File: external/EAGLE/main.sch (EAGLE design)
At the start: 3 parts, among them IC1 AD590ZR

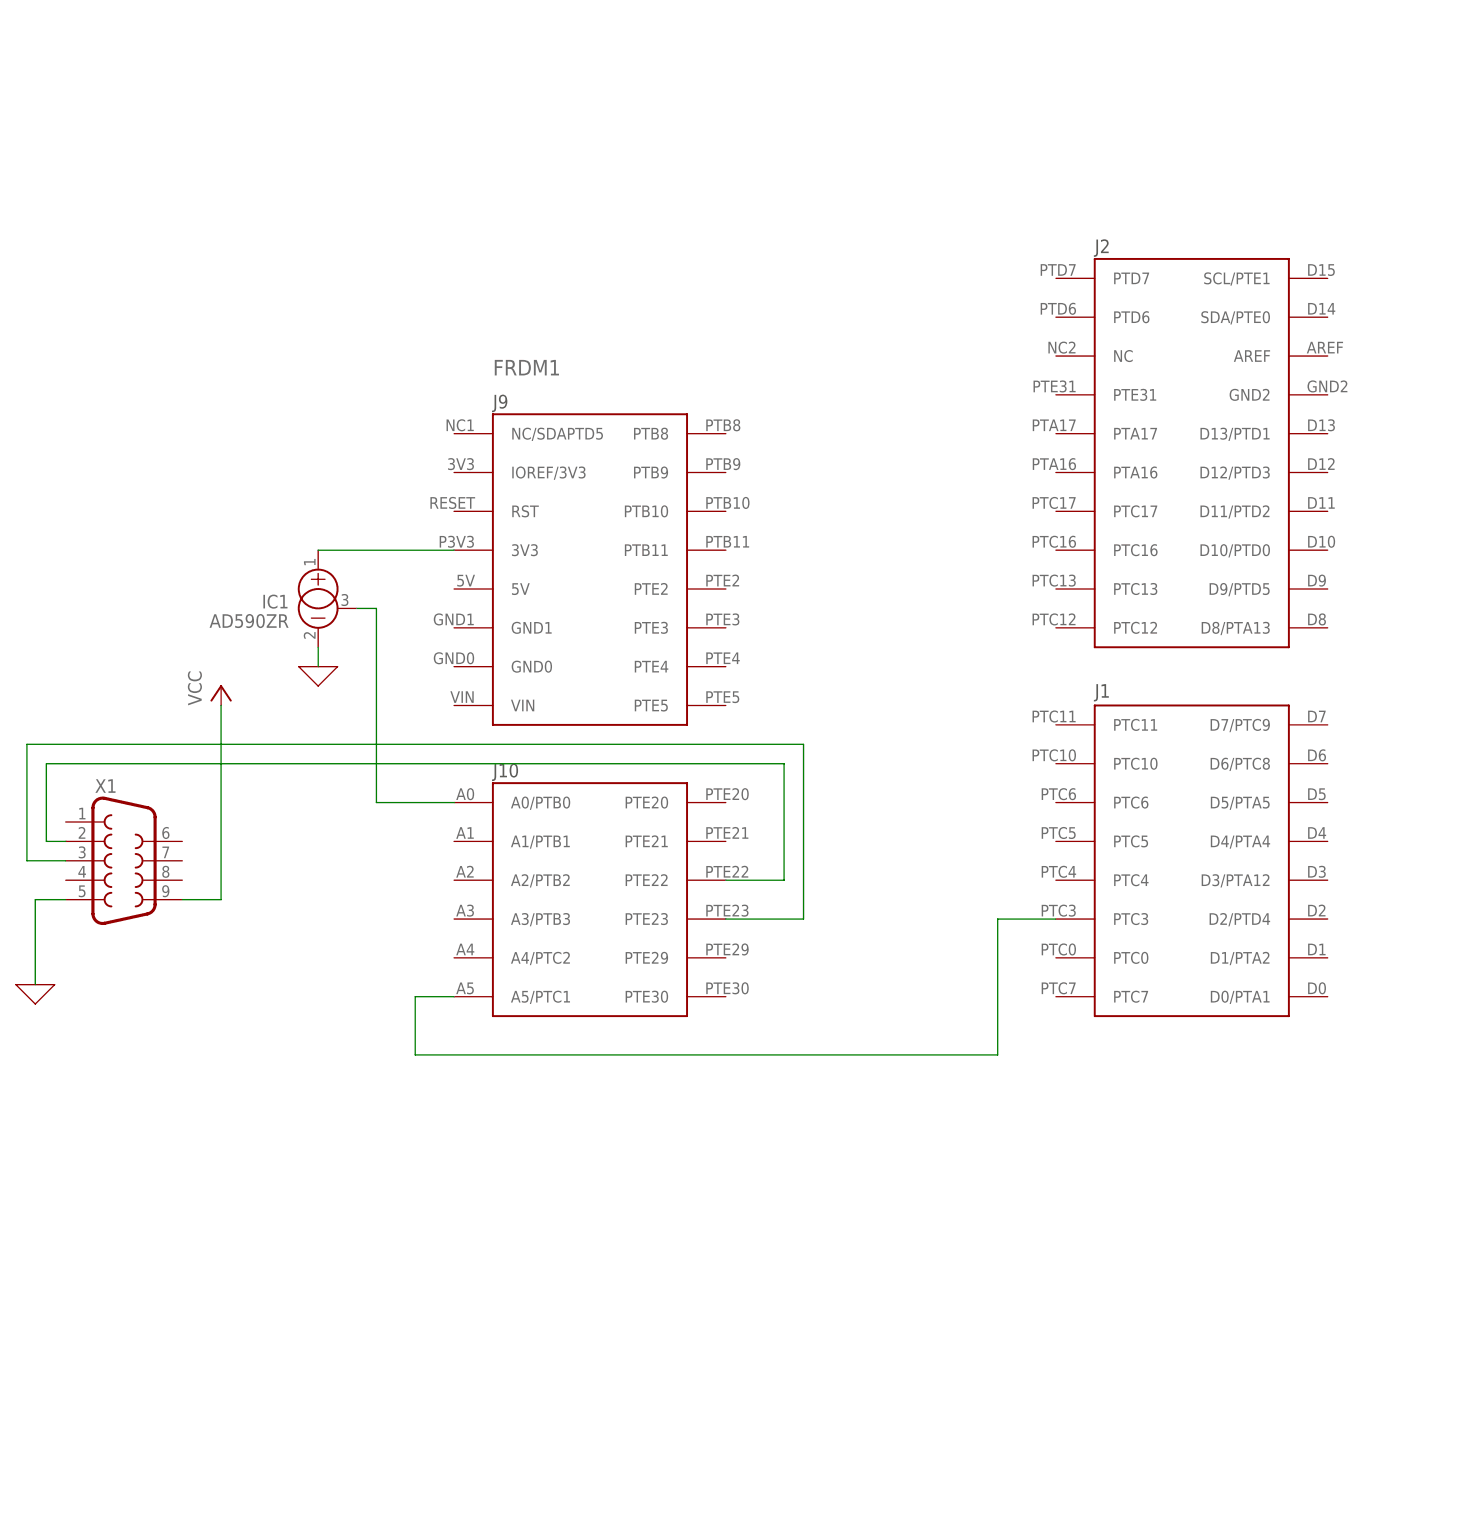
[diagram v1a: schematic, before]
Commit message: Updating the EAGLE schematic
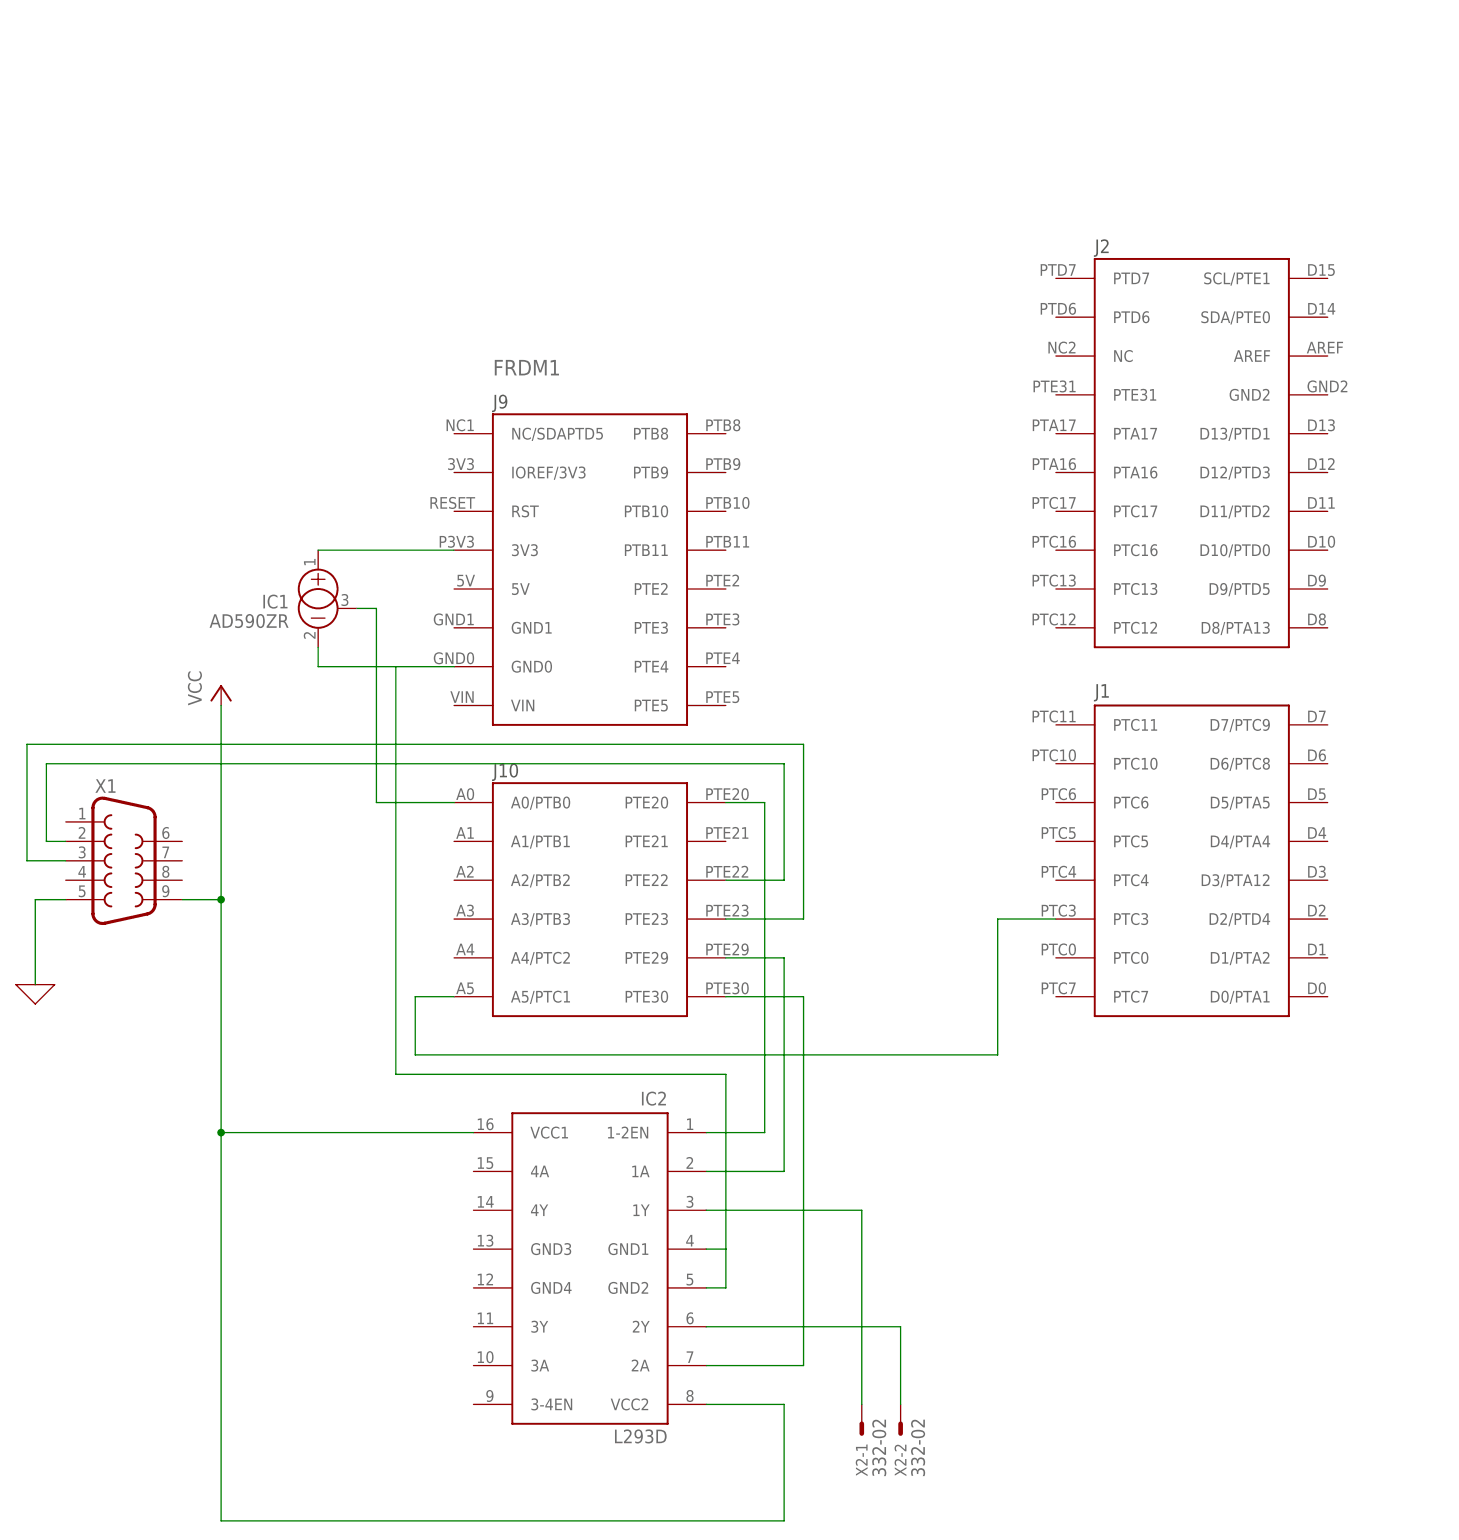
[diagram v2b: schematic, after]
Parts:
- added IC2: L293D, st-microelectronics:L293D
- added X2: 332-02, con-garry:332-02
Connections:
- new net N$10: IC2.2Y, X2-2.S
- new net N$11: FRDM1.GND0, IC1.-, IC2.GND1, IC2.GND2
- new net N$5: IC2.1Y, X2-1.S
- new net N$7: FRDM1.PTE20, IC2.1-2EN
- new net N$8: FRDM1.PTE29, IC2.1A
- new net N$9: FRDM1.PTE30, IC2.2A
- net 0: no longer IC1.-
- net VCC: now also IC2.VCC1, IC2.VCC2
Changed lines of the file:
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@@
 <part name="P+1" library="supply1" library_urn="urn:adsk.eagle:library:371" deviceset="VCC" device=""/>
 <part name="IC1" library="linear" library_urn="urn:adsk.eagle:library:262" deviceset="AD590ZR" device="" package3d_urn="urn:adsk.eagle:package:16416/2"/>
-<part name="X_2" library="ngspice-simulation" library_urn="urn:adsk.eagle:library:527439" deviceset="GND" device=""/>
+<part name="IC2" library="st-microelectronics" library_urn="urn:adsk.eagle:library:368" deviceset="L293D" device="" package3d_urn="urn:adsk.eagle:package:26820/1"/>
+<part name="X2" library="con-garry" library_urn="urn:adsk.eagle:library:147" deviceset="332-02" device="" package3d_urn="urn:adsk.eagle:package:6810/1"/>
 </parts>
 <sheets>
@@
 <attribute name="VALUE" x="44.45" y="-12.7" size="1.778" layer="96" rot="MR0"/>
 </instance>
-<instance part="X_2" gate="G$1" x="48.26" y="-17.78" smashed="yes"/>
+<instance part="IC2" gate="G$1" x="83.82" y="-96.52" smashed="yes" rot="MR0">
+<attribute name="NAME" x="93.98" y="-75.184" size="1.778" layer="95" rot="MR0"/>
+<attribute name="VALUE" x="93.98" y="-119.38" size="1.778" layer="96" rot="MR0"/>
+</instance>
+<instance part="X2" gate="-1" x="119.38" y="-116.84" smashed="yes" rot="R270">
+<attribute name="NAME" x="118.618" y="-119.38" size="1.524" layer="95" rot="R270"/>
+<attribute name="VALUE" x="120.777" y="-116.078" size="1.778" layer="96" rot="R270"/>
+</instance>
+<instance part="X2" gate="-2" x="124.46" y="-116.84" smashed="yes" rot="R270">
+<attribute name="NAME" x="123.698" y="-119.38" size="1.524" layer="95" rot="R270"/>
+<attribute name="VALUE" x="125.857" y="-116.078" size="1.778" layer="96" rot="R270"/>
+</instance>
 </instances>
 <busses>
@@
 <wire x1="11.24940625" y1="-48.26" x2="15.24" y2="-48.26" width="0.1524" layer="91"/>
 </segment>
-<segment>
-<pinref part="X_2" gate="G$1" pin="0"/>
-<pinref part="IC1" gate="A" pin="-"/>
-<wire x1="48.26" y1="-17.78" x2="48.26" y2="-15.24" width="0.1524" layer="91"/>
-</segment>
 </net>
 <net name="VCC" class="0">
@@
 <wire x1="30.48" y1="-48.26" x2="35.56" y2="-48.26" width="0.1524" layer="91"/>
 <wire x1="35.56" y1="-48.26" x2="35.56" y2="-22.86" width="0.1524" layer="91"/>
+<pinref part="IC2" gate="G$1" pin="VCC1"/>
+<wire x1="35.56" y1="-48.26" x2="35.56" y2="-78.74" width="0.1524" layer="91"/>
+<wire x1="35.56" y1="-78.74" x2="68.58" y2="-78.74" width="0.1524" layer="91"/>
+<junction x="35.56" y="-48.26"/>
+<pinref part="IC2" gate="G$1" pin="VCC2"/>
+<wire x1="99.06" y1="-114.3" x2="109.22" y2="-114.3" width="0.1524" layer="91"/>
+<wire x1="109.22" y1="-114.3" x2="109.22" y2="-129.54" width="0.1524" layer="91"/>
+<wire x1="109.22" y1="-129.54" x2="35.56" y2="-129.54" width="0.1524" layer="91"/>
+<wire x1="35.56" y1="-129.54" x2="35.56" y2="-78.74" width="0.1524" layer="91"/>
+<junction x="35.56" y="-78.74"/>
 </segment>
 </net>
@@
 </segment>
 </net>
+<net name="N$7" class="0">
+<segment>
+<pinref part="FRDM1" gate="G$1" pin="PTE20"/>
+<wire x1="101.6" y1="-35.56" x2="106.68" y2="-35.56" width="0.1524" layer="91"/>
+<wire x1="106.68" y1="-35.56" x2="106.68" y2="-78.74" width="0.1524" layer="91"/>
+<pinref part="IC2" gate="G$1" pin="1-2EN"/>
+<wire x1="106.68" y1="-78.74" x2="99.06" y2="-78.74" width="0.1524" layer="91"/>
+</segment>
+</net>
+<net name="N$8" class="0">
+<segment>
+<pinref part="FRDM1" gate="G$1" pin="PTE29"/>
+<wire x1="101.6" y1="-55.88" x2="109.22" y2="-55.88" width="0.1524" layer="91"/>
+<wire x1="109.22" y1="-55.88" x2="109.22" y2="-83.82" width="0.1524" layer="91"/>
+<pinref part="IC2" gate="G$1" pin="1A"/>
+<wire x1="109.22" y1="-83.82" x2="99.06" y2="-83.82" width="0.1524" layer="91"/>
+</segment>
+</net>
+<net name="N$9" class="0">
+<segment>
+<wire x1="111.76" y1="-109.22" x2="111.76" y2="-60.96" width="0.1524" layer="91"/>
+<pinref part="FRDM1" gate="G$1" pin="PTE30"/>
+<wire x1="111.76" y1="-60.96" x2="101.6" y2="-60.96" width="0.1524" layer="91"/>
+<pinref part="IC2" gate="G$1" pin="2A"/>
+<wire x1="111.76" y1="-109.22" x2="99.06" y2="-109.22" width="0.1524" layer="91"/>
+</segment>
+</net>
+<net name="N$5" class="0">
+<segment>
+<pinref part="IC2" gate="G$1" pin="1Y"/>
+<wire x1="99.06" y1="-88.9" x2="119.38" y2="-88.9" width="0.1524" layer="91"/>
+<pinref part="X2" gate="-1" pin="S"/>
+<wire x1="119.38" y1="-88.9" x2="119.38" y2="-114.3" width="0.1524" layer="91"/>
+</segment>
+</net>
+<net name="N$10" class="0">
+<segment>
+<pinref part="IC2" gate="G$1" pin="2Y"/>
+<pinref part="X2" gate="-2" pin="S"/>
+<wire x1="99.06" y1="-104.14" x2="124.46" y2="-104.14" width="0.1524" layer="91"/>
+<wire x1="124.46" y1="-104.14" x2="124.46" y2="-114.3" width="0.1524" layer="91"/>
+</segment>
+</net>
+<net name="N$11" class="0">
+<segment>
+<pinref part="IC2" gate="G$1" pin="GND1"/>
+<wire x1="99.06" y1="-93.98" x2="101.6" y2="-93.98" width="0.1524" layer="91"/>
+<wire x1="101.6" y1="-93.98" x2="101.6" y2="-99.06" width="0.1524" layer="91"/>
+<pinref part="IC2" gate="G$1" pin="GND2"/>
+<wire x1="101.6" y1="-99.06" x2="99.06" y2="-99.06" width="0.1524" layer="91"/>
+<wire x1="101.6" y1="-93.98" x2="101.6" y2="-71.12" width="0.1524" layer="91"/>
+<pinref part="FRDM1" gate="G$1" pin="GND0"/>
+<wire x1="66.04" y1="-17.78" x2="58.42" y2="-17.78" width="0.1524" layer="91"/>
+<wire x1="58.42" y1="-17.78" x2="58.42" y2="-71.12" width="0.1524" layer="91"/>
+<wire x1="58.42" y1="-71.12" x2="101.6" y2="-71.12" width="0.1524" layer="91"/>
+<pinref part="IC1" gate="A" pin="-"/>
+<wire x1="48.26" y1="-15.24" x2="48.26" y2="-17.78" width="0.1524" layer="91"/>
+<wire x1="48.26" y1="-17.78" x2="58.42" y2="-17.78" width="0.1524" layer="91"/>
+</segment>
+</net>

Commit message: Uploading the schematic with NOKIA 5110 LCD Display connections
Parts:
- added J1: 1-794681-6, con-amp:1-794681-6
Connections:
- new net N$12: FRDM1.PTE3, J1.15
- new net N$13: FRDM1.PTE5, J1.11
- new net N$14: FRDM1.PTE4, J1.13
- new net N$15: FRDM1.PTE2, J1.3
- new net N$16: FRDM1.PTC6, J1.9
- new net N$17: FRDM1.PTC5, J1.7
- net N$11: now also J1.1
- net N$6: now also J1.5
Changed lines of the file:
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@@
 <part name="IC2" library="st-microelectronics" library_urn="urn:adsk.eagle:library:368" deviceset="L293D" device="" package3d_urn="urn:adsk.eagle:package:26820/1"/>
 <part name="X2" library="con-garry" library_urn="urn:adsk.eagle:library:147" deviceset="332-02" device="" package3d_urn="urn:adsk.eagle:package:6810/1"/>
+<part name="J1" library="con-amp" library_urn="urn:adsk.eagle:library:127" deviceset="1-794681-6" device=""/>
 </parts>
 <sheets>
@@
 <attribute name="NAME" x="123.698" y="-119.38" size="1.524" layer="95" rot="R270"/>
 <attribute name="VALUE" x="125.857" y="-116.078" size="1.778" layer="96" rot="R270"/>
+</instance>
+<instance part="J1" gate="G$1" x="114.3" y="33.02" smashed="yes" rot="R90">
+<attribute name="NAME" x="128.27" y="27.94" size="1.778" layer="95" rot="R90"/>
+<attribute name="VALUE" x="104.14" y="27.94" size="1.778" layer="96" rot="R90"/>
 </instance>
 </instances>
@@
 <pinref part="IC1" gate="A" pin="+"/>
 <pinref part="FRDM1" gate="G$1" pin="3V3"/>
-<wire x1="66.04" y1="-2.54" x2="48.26" y2="-2.54" width="0.1524" layer="91"/>
+<wire x1="66.04" y1="-2.54" x2="60.96" y2="-2.54" width="0.1524" layer="91"/>
+<pinref part="J1" gate="G$1" pin="5"/>
+<wire x1="60.96" y1="-2.54" x2="48.26" y2="-2.54" width="0.1524" layer="91"/>
+<wire x1="119.38" y1="27.94" x2="119.38" y2="22.86" width="0.1524" layer="91"/>
+<wire x1="119.38" y1="22.86" x2="60.96" y2="22.86" width="0.1524" layer="91"/>
+<wire x1="60.96" y1="22.86" x2="60.96" y2="-2.54" width="0.1524" layer="91"/>
+<junction x="60.96" y="-2.54"/>
 </segment>
 </net>
@@
 <wire x1="48.26" y1="-15.24" x2="48.26" y2="-17.78" width="0.1524" layer="91"/>
 <wire x1="48.26" y1="-17.78" x2="58.42" y2="-17.78" width="0.1524" layer="91"/>
-</segment>
-</net>
+<wire x1="58.42" y1="-17.78" x2="58.42" y2="25.4" width="0.1524" layer="91"/>
+<wire x1="58.42" y1="25.4" x2="124.46" y2="25.4" width="0.1524" layer="91"/>
+<pinref part="J1" gate="G$1" pin="1"/>
+<wire x1="124.46" y1="25.4" x2="124.46" y2="27.94" width="0.1524" layer="91"/>
+</segment>
+</net>
+<net name="N$12" class="0">
+<segment>
+<pinref part="J1" gate="G$1" pin="15"/>
+<pinref part="FRDM1" gate="G$1" pin="PTE3"/>
+<wire x1="106.68" y1="27.94" x2="106.68" y2="-12.7" width="0.1524" layer="91"/>
+<wire x1="106.68" y1="-12.7" x2="101.6" y2="-12.7" width="0.1524" layer="91"/>
+</segment>
+</net>
+<net name="N$13" class="0">
+<segment>
+<pinref part="J1" gate="G$1" pin="11"/>
+<wire x1="111.76" y1="27.94" x2="111.76" y2="-22.86" width="0.1524" layer="91"/>
+<pinref part="FRDM1" gate="G$1" pin="PTE5"/>
+<wire x1="111.76" y1="-22.86" x2="101.6" y2="-22.86" width="0.1524" layer="91"/>
+</segment>
+</net>
+<net name="N$14" class="0">
+<segment>
+<pinref part="J1" gate="G$1" pin="13"/>
+<pinref part="FRDM1" gate="G$1" pin="PTE4"/>
+<wire x1="109.22" y1="27.94" x2="109.22" y2="-17.78" width="0.1524" layer="91"/>
+<wire x1="109.22" y1="-17.78" x2="101.6" y2="-17.78" width="0.1524" layer="91"/>
+</segment>
+</net>
+<net name="N$15" class="0">
+<segment>
+<pinref part="J1" gate="G$1" pin="3"/>
+<pinref part="FRDM1" gate="G$1" pin="PTE2"/>
+<wire x1="121.92" y1="27.94" x2="121.92" y2="-7.62" width="0.1524" layer="91"/>
+<wire x1="121.92" y1="-7.62" x2="101.6" y2="-7.62" width="0.1524" layer="91"/>
+</segment>
+</net>
+<net name="N$17" class="0">
+<segment>
+<pinref part="J1" gate="G$1" pin="7"/>
+<pinref part="FRDM1" gate="G$1" pin="PTC5"/>
+<wire x1="116.84" y1="27.94" x2="116.84" y2="-40.64" width="0.1524" layer="91"/>
+<wire x1="116.84" y1="-40.64" x2="144.78" y2="-40.64" width="0.1524" layer="91"/>
+</segment>
+</net>
+<net name="N$16" class="0">
+<segment>
+<pinref part="FRDM1" gate="G$1" pin="PTC6"/>
+<wire x1="144.78" y1="-35.56" x2="114.3" y2="-35.56" width="0.1524" layer="91"/>
+<pinref part="J1" gate="G$1" pin="9"/>
+<wire x1="114.3" y1="-35.56" x2="114.3" y2="27.94" width="0.1524" layer="91"/>
+</segment>
+</net>
